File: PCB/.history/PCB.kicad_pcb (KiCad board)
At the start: 2 copper layers, 62 parts, among them J1 USB_C_Receptacle_USB2.0_14P, J2 OLED_128x64, SW1 SW_Push, U1 STM32F072CBTx, U2 USBLC6-2SC6, U3 XC6206, U5 TRRS

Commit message: Added rotatry knobs to sketch
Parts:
- added R4: 10k, Resistor_SMD:R_0805_2012Metric, F.Cu at (184.5, 85.5)
- added R5: 10k, Resistor_SMD:R_0805_2012Metric, F.Cu at (184.5, 88.4)
- added R6: 10k, Resistor_SMD:R_0805_2012Metric, F.Cu at (184.5, 91.4)
- added R7: 10k, Resistor_SMD:R_0805_2012Metric, F.Cu at (184.5, 94.3)
- added SW2: RotaryEncoder, Rotary_Encoder:RotaryEncoder_Alps_EC11E_Vertical_H20mm, F.Cu at (166.3, 88.9)
- added SW3: RotaryEncoder, Rotary_Encoder:RotaryEncoder_Alps_EC11E_Vertical_H20mm, F.Cu at (166.3, 103.6)
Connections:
- U1 pad 10: unconnected-(U1-PA0-Pad10) -> RE_1_A
- U1 pad 11: unconnected-(U1-PA1-Pad11) -> RE_1_B
- U1 pad 12: unconnected-(U1-PA2-Pad12) -> RE_1_B
- U1 pad 17: unconnected-(U1-PA7-Pad17) -> RE_2_A
- U1 pad 29: unconnected-(U1-PA8-Pad29) -> RE_2_B

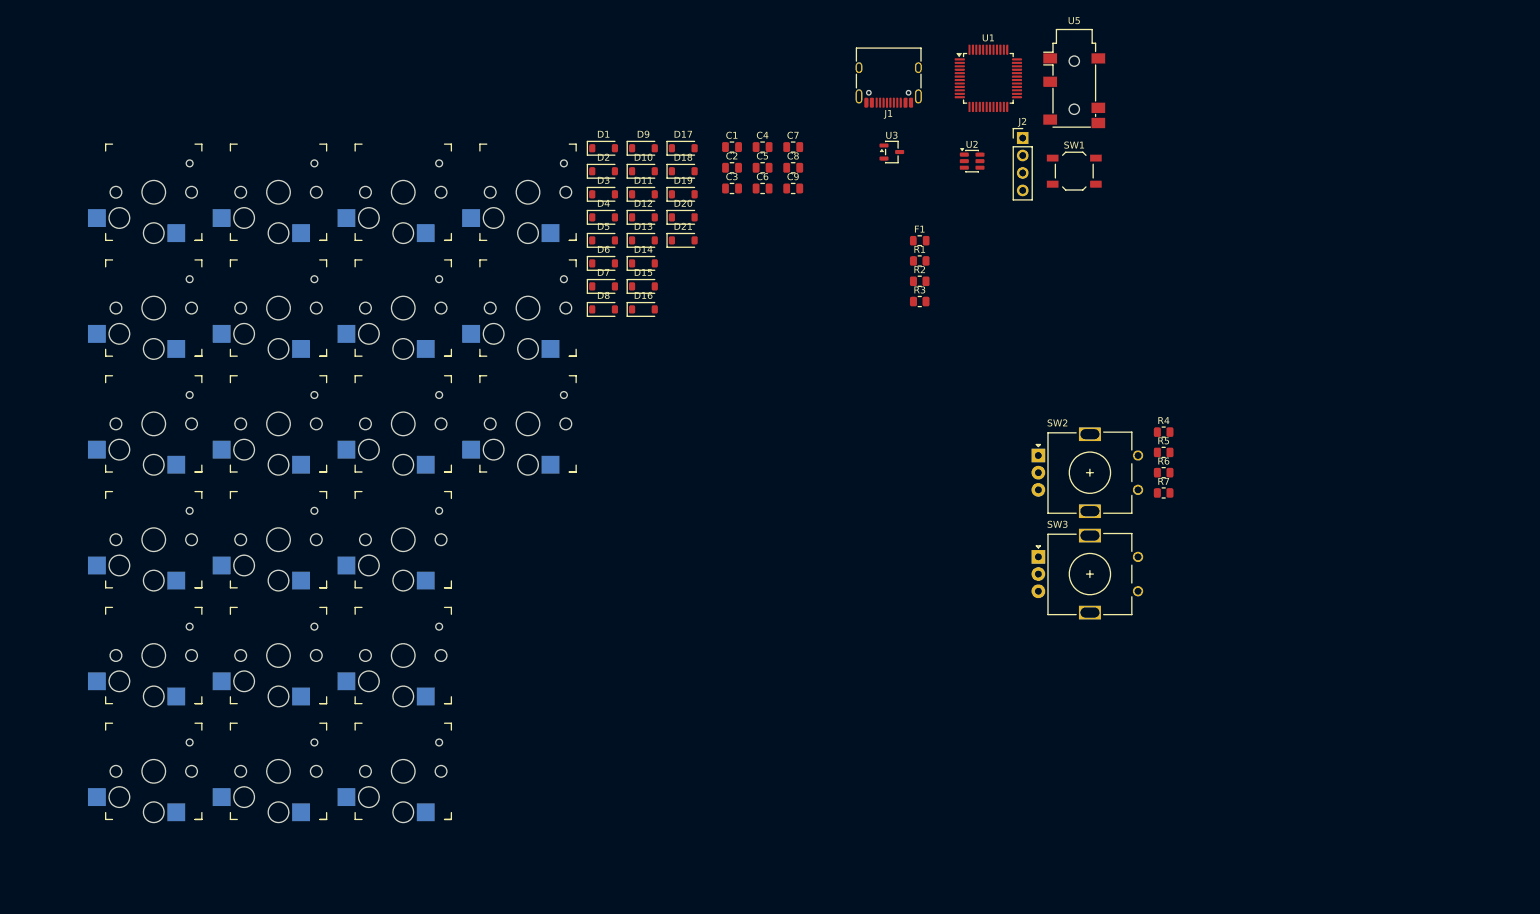
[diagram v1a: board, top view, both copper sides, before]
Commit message: Done with the kiCad Matrix layout placement in sketch
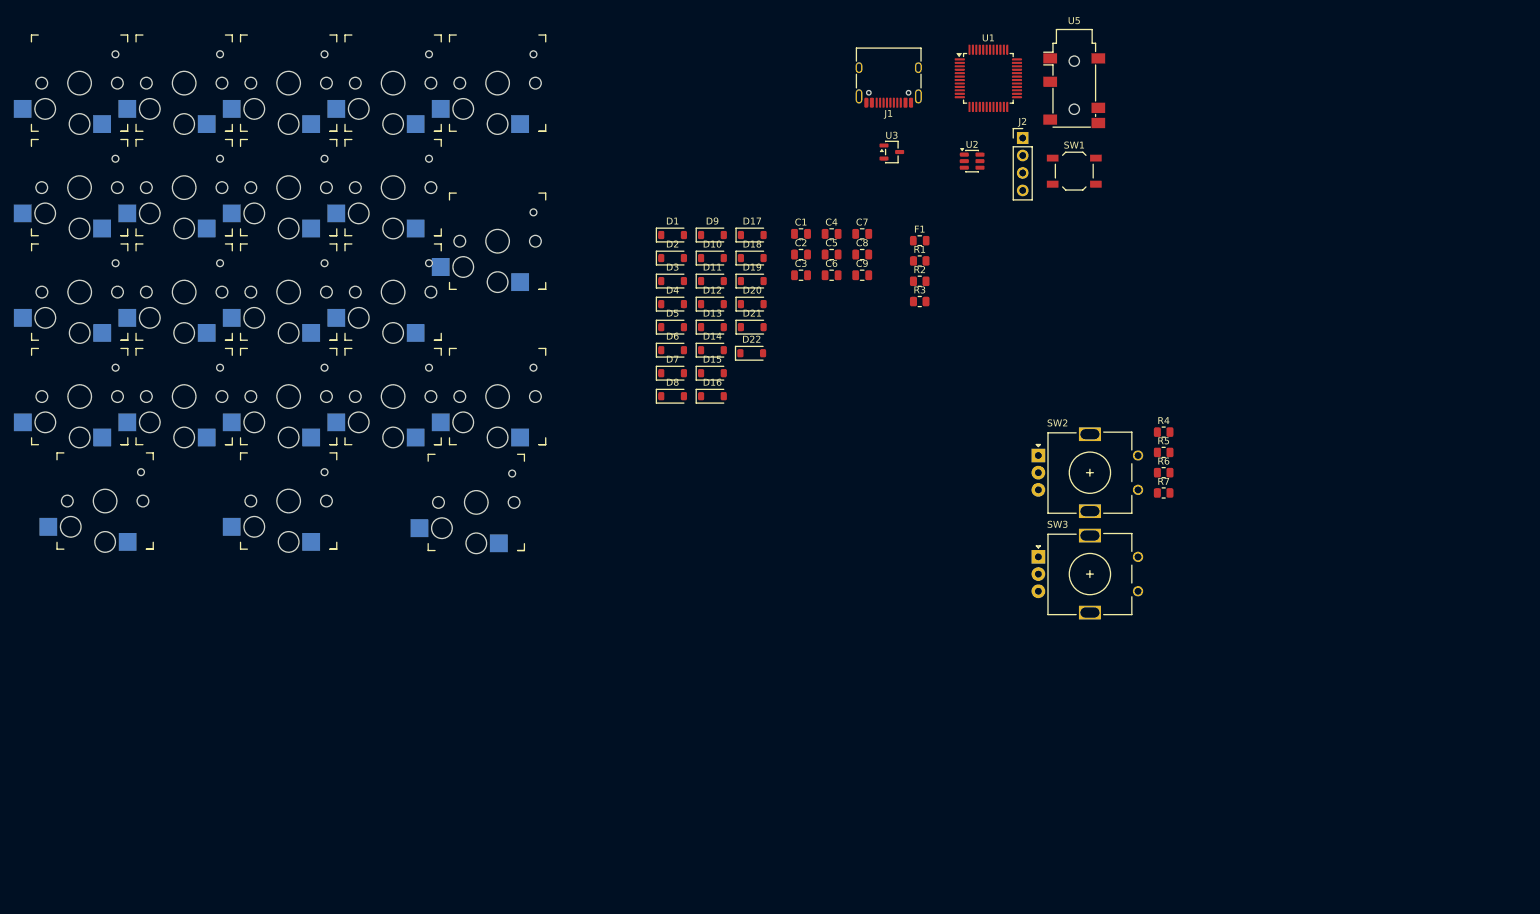
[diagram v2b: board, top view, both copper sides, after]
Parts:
- added D22: ~, Diode_SMD:D_SOD-123, F.Cu at (124.6, 74.0)
- added S22: ~, Keyboard switches:Kailh_socket_PG1350, F.Cu at (87.6, 80.3)
- moved S5 97.1 mm to (87.6, 34.7)
- moved S6 85.6 mm to (26.8, 49.9)
- moved S19 76.2 mm to (30.5, 95.5)
- moved S4 75.0 mm to (72.4, 34.7)
- moved S12 71.1 mm to (42.0, 65.1)
- moved S11 60.3 mm to (26.8, 65.1)
- moved S18 54.5 mm to (72.4, 80.3)
- moved S10 53.9 mm to (87.6, 57.7)
- moved S3 53.3 mm to (57.2, 34.7)
- moved S15 47.2 mm to (26.8, 80.3)
- moved S20 44.7 mm to (57.2, 95.5)
- moved S17 41.2 mm to (57.2, 80.3)
- moved S9 38.2 mm to (72.4, 49.9)
- moved S16 38.1 mm to (42.0, 80.3)
- moved S2 33.0 mm to (42.0, 34.7)
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
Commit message: Finally done orchestrating and placing of component on PCB
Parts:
- D1, D10, D11, D12, D13, D14, D15, D16, D17, D18, D19, D2, D20, D21, D22, D3, D4, D5, D6, D7, D8, D9: moved to B.Cu
- moved R6 148.0 mm to (41.5, 53.1), turned to 90 degrees
- moved R7 144.5 mm to (46.0, 53.1), turned to 90 degrees
- moved SW3 141.4 mm to (41.0, 38.0)
- moved R4 130.8 mm to (58.0, 52.4), turned to 90 degrees
- moved R5 127.2 mm to (62.5, 52.4), turned to 90 degrees
- moved SW2 119.6 mm to (58.0, 38.0)
- moved D19 93.4 mm to (55.3, 126.1), turned to 90 degrees
- moved SW1 77.2 mm to (94.5, 41.3)
- moved U1 75.8 mm to (85.0, 50.5)
- moved D15 75.5 mm to (51.3, 110.6), turned to 90 degrees
- moved D11 74.8 mm to (51.3, 95.6), turned to 90 degrees
- moved U2 73.9 mm to (82.9, 42.5)
- moved D20 73.1 mm to (81.8, 126.1), turned to 90 degrees
- moved D17 68.8 mm to (81.8, 110.6), turned to 90 degrees
- moved U3 68.5 mm to (76.5, 44.9), turned to 90 degrees
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
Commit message: GGs finally fucking finished routing the retardly dense clustered traces now i understand why em electronic board based prods so expensive gng
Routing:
- net GND: track 0.00 -> 251.5 mm, vias 0 -> 19
- net +3.3V: track 0.00 -> 199.7 mm, vias 0 -> 23
- net R4: track 0.00 -> 174.8 mm, vias 0 -> 11
- net R3: track 0.00 -> 154.1 mm, vias 0 -> 11
- net R1: track 0.00 -> 117.1 mm, vias 0 -> 11
- net C1: track 0.00 -> 114.7 mm, vias 0 -> 3
- net R2: track 0.00 -> 112.5 mm, vias 0 -> 11
- net C0: track 0.00 -> 111.4 mm, vias 0 -> 1
- net R0: track 0.00 -> 108.1 mm, vias 0 -> 13
- net C2: track 0.00 -> 105.4 mm, vias 0 -> 3
- net C4: track 0.00 -> 84.5 mm, vias 0 -> 1
- net C3: track 0.00 -> 73.2 mm, vias 0 -> 3
- net D-: track 0.00 -> 73.0 mm, vias 0 -> 9
- net RE_2_B: track 0.00 -> 64.0 mm, vias 0 -> 8
- net RE_2_A: track 0.00 -> 55.4 mm, vias 0 -> 4
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
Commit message: Finally DCR check passed
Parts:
- moved S10 0.40 mm to (109.3, 86.8)
- moved S22 0.40 mm to (109.3, 109.4)
- moved S5 0.40 mm to (109.3, 63.8)
- moved D10 0.30 mm to (112.4, 88.2)
- moved D5 0.30 mm to (112.4, 64.8)
- moved D22 0.10 mm to (112.4, 110.6)
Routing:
- net C4: track 84.5 -> 85.6 mm
- net RE_1_A: vias 5 -> 4
- net GND: vias 19 -> 17
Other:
- board outline added: 82.5 x 104.5 mm

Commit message: Updated the PCB with proper alignments and design decisions
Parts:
- moved S10 3.80 mm to (109.9, 90.5)
- moved S5 3.80 mm to (109.9, 67.5)
- moved D5 3.37 mm to (113.3, 68.0)
- moved D10 1.97 mm to (113.3, 90.0)
- moved D22 0.90 mm to (113.3, 110.6)
- moved S22 0.60 mm to (109.9, 109.4)
- moved D21 0.60 mm to (108.3, 125.5)
- moved S21 0.05 mm to (105.2, 124.6)
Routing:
- net C4: track 85.6 -> 92.0 mm
- net C2: track 105.4 -> 100.5 mm
- net Net-(D10-A): track 14.0 -> 17.8 mm
- net R1: track 117.1 -> 120.8 mm
- net R0: track 108.1 -> 111.5 mm
- net Net-(D5-A): track 14.3 -> 17.5 mm
- net R4: track 174.8 -> 177.3 mm
- net +3.3V: track 199.5 -> 197.7 mm
- net Net-(D22-A): track 14.6 -> 15.8 mm
- net Net-(D21-A): track 13.6 -> 14.8 mm, vias 0 -> 2
- net R3: track 154.1 -> 155.1 mm
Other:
- board size 82.5 x 104.5 mm -> 84 x 105 mm

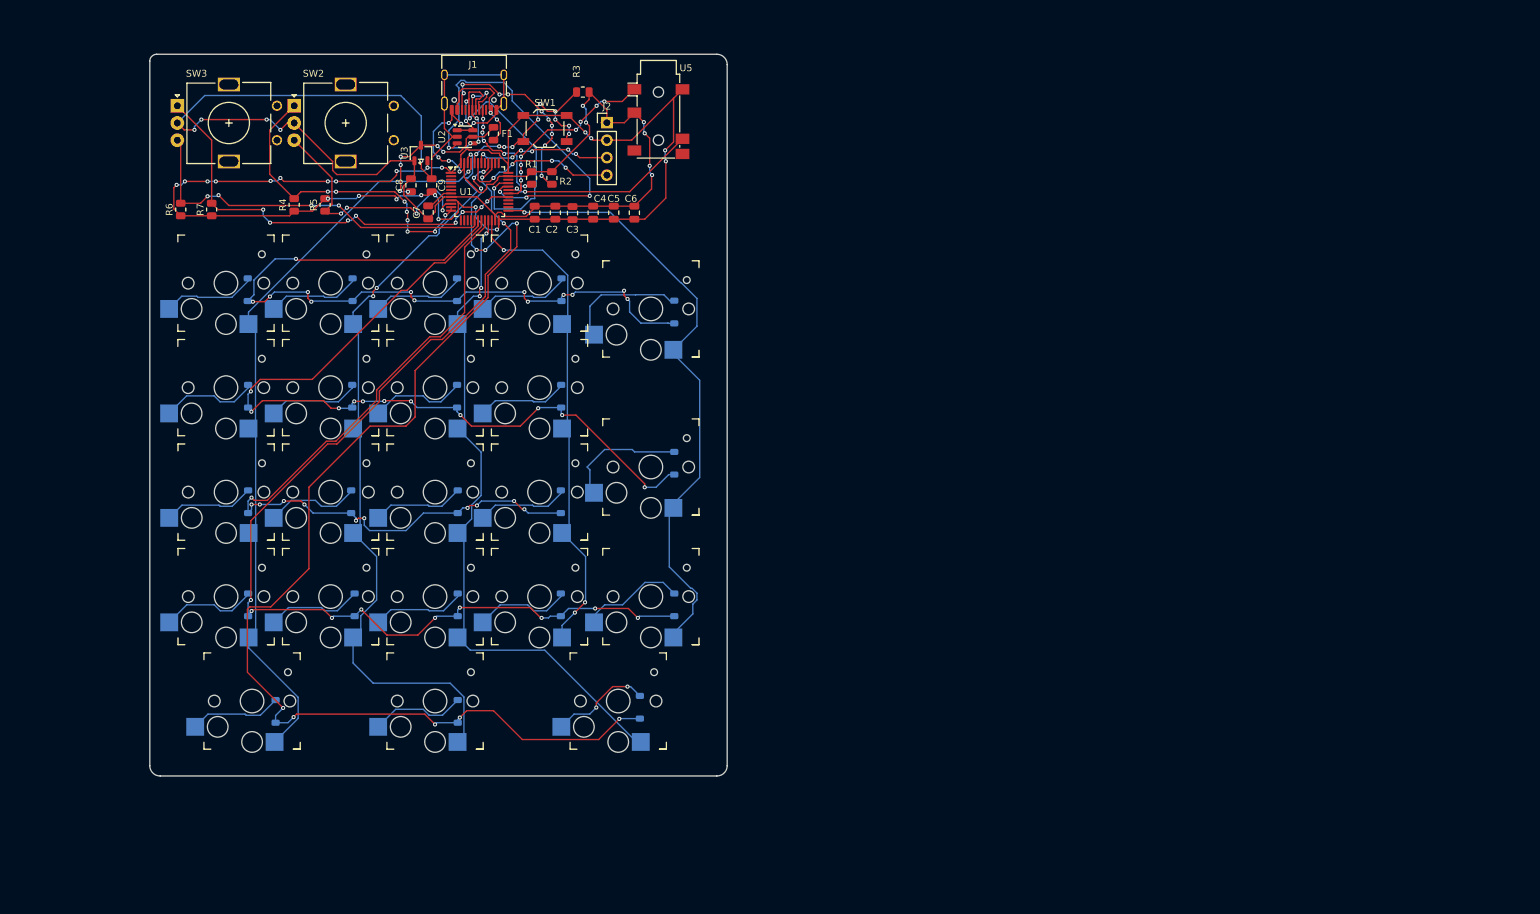
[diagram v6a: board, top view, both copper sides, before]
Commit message: Improved routing and the first final iteration of PCB
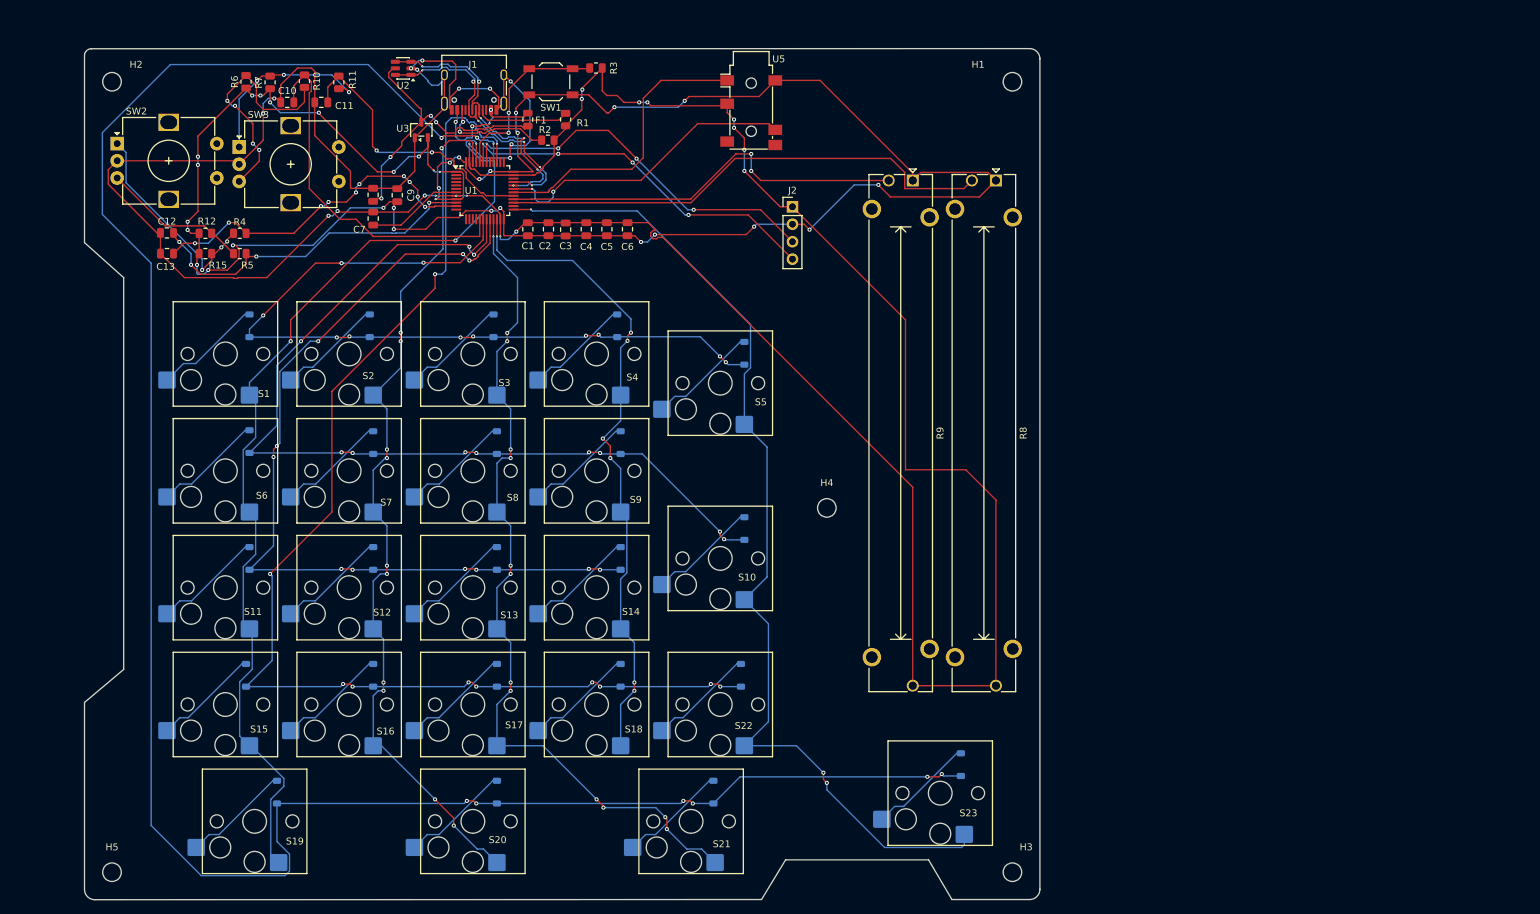
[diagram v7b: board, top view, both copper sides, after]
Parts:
- added C10: 10nF, Capacitor_SMD:C_0805_2012Metric, F.Cu at (57.0, 37.5)
- added C11: 10nF, Capacitor_SMD:C_0805_2012Metric, F.Cu at (62.0, 37.5)
- added C12: 10nF, Capacitor_SMD:C_0805_2012Metric, F.Cu at (39.5, 56.5)
- added C13: 10nF, Capacitor_SMD:C_0805_2012Metric, F.Cu at (39.5, 59.5)
- added D23: ~, Diode_SMD:D_SOD-123, B.Cu at (155.0, 133.8)
- added H1: MountingHole, MountingHole:MountingHole_2.7mm, F.Cu at (162.5, 34.5)
- added H2: MountingHole, MountingHole:MountingHole_2.7mm, F.Cu at (31.5, 34.5)
- added H3: MountingHole, MountingHole:MountingHole_2.7mm, F.Cu at (162.5, 149.5)
- added H4: MountingHole, MountingHole:MountingHole_2.7mm, F.Cu at (135.5, 96.5)
- added H5: MountingHole, MountingHole:MountingHole_2.7mm, F.Cu at (31.5, 149.5)
- added R10: 10k, Resistor_SMD:R_0805_2012Metric, F.Cu at (59.5, 34.4)
- added R11: 10k, Resistor_SMD:R_0805_2012Metric, F.Cu at (64.5, 34.6)
- added R12: 10k, Resistor_SMD:R_0805_2012Metric, F.Cu at (45.1, 56.5)
- added R15: 10k, Resistor_SMD:R_0805_2012Metric, F.Cu at (45.1, 59.5)
- added R8: Potentiometer, Potentiometer_THT:Potentiometer_Bourns_PTA6043_Single_Slide, F.Cu at (160.1, 48.9)
- added R9: Potentiometer, Potentiometer_THT:Potentiometer_Bourns_PTA6043_Single_Slide, F.Cu at (148.0, 48.9)
- added S23: ~, ScottoKeebs_Choc:Hotswap_Choc_V1_1.00u, F.Cu at (152.0, 138.0)
- S1, S10, S11, S12, S13, S14, S15, S16, S17, S18, S19, S2, S20, S21, S22, S3, S4, S5, S6, S7, S8, S9: footprint Keyboard switches:Kailh_socket_PG1350 -> ScottoKeebs_Choc:Hotswap_Choc_V1_1.00u
- SW2, SW3: footprint Rotary_Encoder:RotaryEncoder_Alps_EC11E_Vertical_H20mm -> Rotary_Encoder:RotaryEncoder_Alps_EC12E-Switch_Vertical_H20mm
- moved J2 29.6 mm to (130.5, 52.7)
- moved SW2 26.3 mm to (32.2, 43.5)
- moved R6 20.9 mm to (51.0, 34.5)
- moved S21 20.5 mm to (115.8, 142.1), turned to 180 degrees
- moved R7 20.4 mm to (54.5, 34.6)
- moved S22 18.7 mm to (120.0, 125.1), turned to 180 degrees
- moved S20 18.3 mm to (84.0, 142.1), turned to 180 degrees
- moved S18 17.8 mm to (102.0, 125.1), turned to 180 degrees
- moved S19 17.5 mm to (52.2, 142.1), turned to 180 degrees
- moved S10 16.7 mm to (120.0, 103.8), turned to 180 degrees
- moved S17 16.6 mm to (84.0, 125.1), turned to 180 degrees
- moved D21 16.3 mm to (119.0, 137.8)
- moved S14 16.2 mm to (102.0, 108.1), turned to 180 degrees
- moved S16 15.9 mm to (66.0, 125.1), turned to 180 degrees
- moved S15 15.7 mm to (48.0, 125.1), turned to 180 degrees
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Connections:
- R4 pad 1: +3.3V -> Net-(R15-Pad2)
- R5 pad 1: RE_1_A -> Net-(R12-Pad2)
- R5 pad 2: +3.3V -> RE_1_A
- R6 pad 2: RE_2_A -> Net-(R10-Pad1)
- R7 pad 2: RE_2_B -> Net-(R11-Pad1)
- SW2 pad A: RE_1_B -> Net-(R15-Pad2)
- SW2 pad B: RE_1_A -> Net-(R12-Pad2)
- SW3 pad A: RE_2_B -> Net-(R11-Pad1)
- SW3 pad B: RE_2_A -> Net-(R10-Pad1)
- U1 pad 12: RE_1_B -> unconnected-(U1-PA2-Pad12)
- U1 pad 27: unconnected-(U1-PB14-Pad27) -> SLIDER_1
- U1 pad 28: unconnected-(U1-PB15-Pad28) -> SLIDER_2
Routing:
- net GND: track 251.5 -> 508.6 mm, vias 17 -> 27
- net +3.3V: track 197.7 -> 338.5 mm, vias 23 -> 35
- net R4: track 177.3 -> 308.6 mm, vias 11 -> 9
- net SLIDER_1: track 0.00 -> 73.0 mm
- net SLIDER_2: track 0.00 -> 60.4 mm, vias 0 -> 2
- net C4: track 92.0 -> 149.7 mm, vias 1 -> 3
- net SCL: track 20.7 -> 55.2 mm, vias 6 -> 4
- net Net-(R10-Pad1): track 0.00 -> 34.4 mm, vias 0 -> 4
- net SDA: track 23.4 -> 54.7 mm
- net Net-(R15-Pad2): track 0.00 -> 31.0 mm, vias 0 -> 3
- net C0: track 111.4 -> 142.1 mm, vias 1 -> 3
- net D-: track 73.0 -> 42.6 mm, vias 9 -> 6
- net Net-(R11-Pad1): track 0.00 -> 27.2 mm, vias 0 -> 3
- net R3: track 155.1 -> 181.7 mm
- net C2: track 100.5 -> 124.8 mm, vias 3 -> 13
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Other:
- board size 84 x 105 mm -> 139 x 123.8 mm
